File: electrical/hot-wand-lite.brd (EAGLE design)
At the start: 112 x 72 mm, 73 parts, among them IC1 12V R-78K12-2.0, IC2 AMS1117-5.0, Q1 NCHAN, Q2 SIRS5800DP-T1-GE3, Q3 DMTH64M2LPDWQ-13, Q4 2N7002K, U1 SEEED-XIAO-SAMD21, U2 1EDN8511BXUSA1, U3 LM74700QDBVTQ1, U4 AP53781

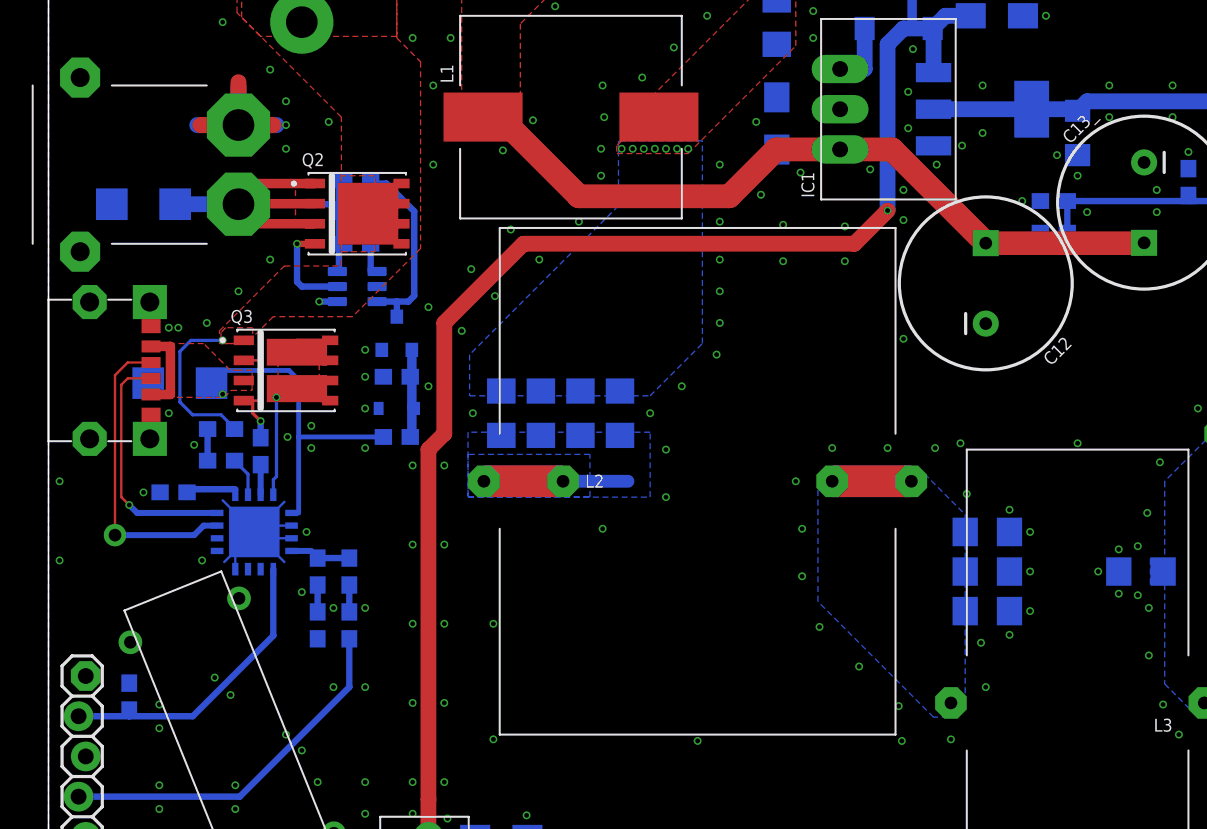
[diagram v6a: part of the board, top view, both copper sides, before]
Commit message: names and part numbers
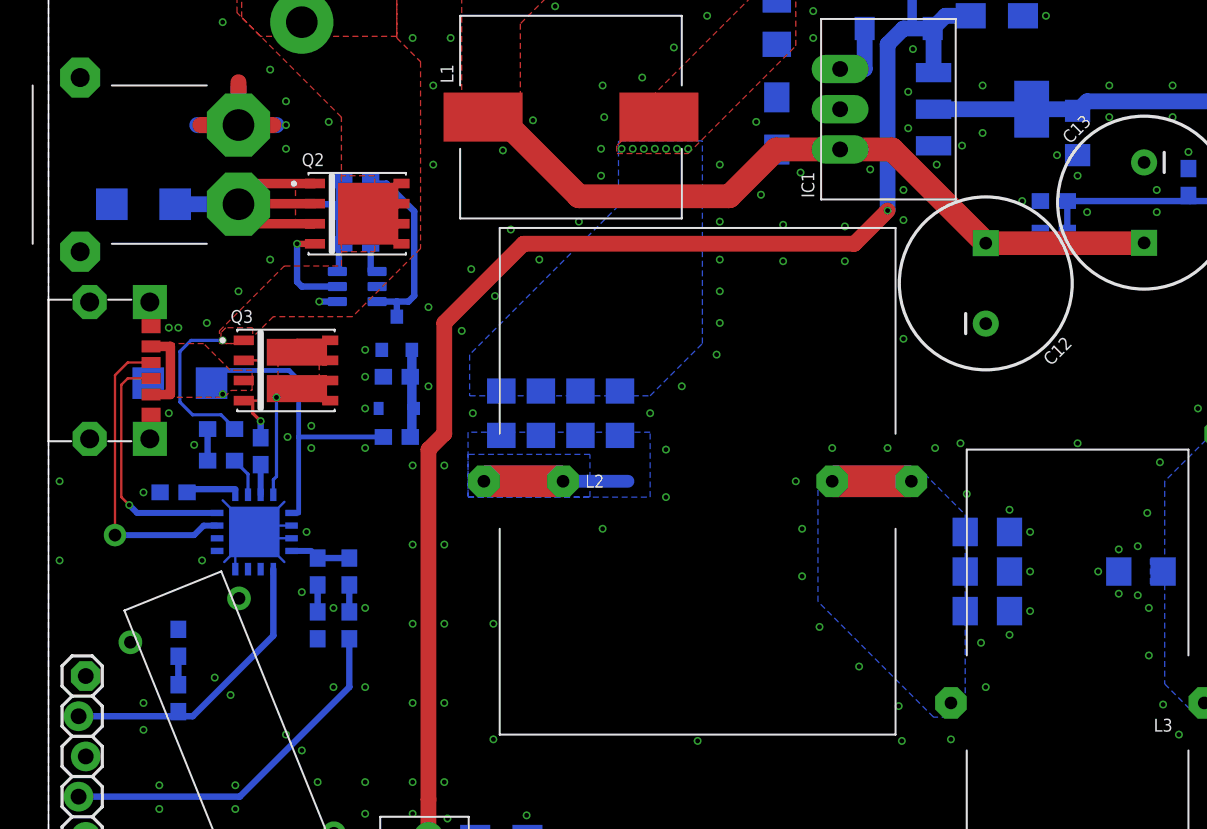
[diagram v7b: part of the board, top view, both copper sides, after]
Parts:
- removed C13_: 470u, hot-wand:CPOL-RADIAL-1000UF-25V
- removed R17_: 1K, hot-wand:0603-RES
- added C23: 100n, hot-wand:0603-CAP
- added R15: 51K, hot-wand:0603-RES
- added R7: 4K7, hot-wand:0603-RES
- C13: value 10u -> 470u; device hot-wand:EIA3216-KIT -> hot-wand:CPOL-RADIAL-1000UF-25V
- C15: device hot-wand:EIA3216 -> hot-wand:EIA3216-KIT
- C16: device hot-wand:EIA3216-KIT -> hot-wand:EIA3216
- C17: value 100n -> 10u; device hot-wand:0603-CAP -> hot-wand:EIA3216-KIT
- C18: value 1uF -> 100n
- C19: value 100n -> 1uF
- R10: value 4K7 -> 100Ω
- R11: value 4K3 -> 100Ω
- R12: value 100Ω -> 4K7
- R13: value 100Ω -> 24K
- R14: value 4K7 -> 2K
- R16: value 51K -> 1K
- R8: value 26K -> 4K7
- R9: value 4K7 -> 4K3
- moved C22 67.0 mm to (7.90, 32.3), turned to 180 degrees
- moved C17 62.1 mm to (28.6, 10.5)
- moved C16 57.5 mm to (65.0, 55.0), turned to 90 degrees
- moved C19 38.8 mm to (55.4, 64.6)
- moved R14 31.3 mm to (8.20, 22.8), turned to 90 degrees
- moved C13 23.7 mm to (69.2, 50.6), flipped to the top
- moved R8 23.5 mm to (22.0, 35.8), turned to 180 degrees
- moved R12 19.7 mm to (19.5, 52.0)
- moved C21 19.5 mm to (19.5, 48.0)
- moved R13 17.2 mm to (8.20, 19.3), turned to 90 degrees
- moved C14 15.5 mm to (46.0, 55.6), turned to 270 degrees
- moved R10 11.2 mm to (10.9, 34.3)
- moved R9 9.80 mm to (13.4, 34.9), turned to 270 degrees
- moved C15 8.99 mm to (59.9, 62.4), turned to 0 degrees
- moved R16 3.40 mm to (17.0, 23.9)
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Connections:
- new net N$10: R13.2, R14.1
- net +12V: now also C15.A, C17.A, C19.2; no longer C14.A, C16.A, C17.2
- net +24V: now also C13.1, C14.A; no longer C13.A, C13_.1
- net 5V: now also C16.A; no longer C15.A
- net ADC: now also C23.2; no longer C22.2
- net DC-SRC: now also R11.1; no longer R13.1
- net GND: now also C13.2, C17.C, C20.1, C23.1, R14.2, R16.2, R7.1; no longer C13.C, C13_.2, C17.1, C21.1, R17_.2, R8.2, R9.1
- net N$30: now also R7.2, R8.2; no longer R10.2, R9.2
- net N$31: now also C20.2, C21.1, R12.1; no longer C19.2, C20.1, R14.1
- net N$32: now also C21.2; no longer C20.2
- net N$36: now also R9.2; no longer R11.2
- net N$37: now also R9.1; no longer R11.1
- net N$38: now also C22.2; no longer C21.2
- net N$39: now also R8.1; no longer R10.1
- net N$40: now also R10.2; no longer R12.2
- net N$42: now also R15.1; no longer R16.1
- net N$43: now also R12.2; no longer R14.2
- net N$57: now also R10.1, R11.2; no longer R12.1, R13.2
- net N$9: now also R15.2, R16.1; no longer R16.2, R17_.1
- net USB-I-SEL: now also R13.1; no longer R8.1
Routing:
- net N$10: track 0.00 -> 1.80 mm

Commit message: lite, meas resistors
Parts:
- added SJ1, SJ2, SJ3, SJ4, SJ5: SJ-SMALL-1206-SJ, hot-wand:1206-SJ
- moved LED1 4.00 mm to (111.0, 45.3)
- moved LED2 4.00 mm to (111.0, 45.3)
- moved R5 4.00 mm to (110.4, 48.3)
- moved R6 4.00 mm to (108.4, 48.3)
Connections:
- new net N$11: Q1.3, Q1.3B, SJ1.2
- new net N$12: JP1.2_1, JP1.2_2, JP1.3_1, JP1.3_2, SJ2.1, SJ3.1, SJ4.1, SJ5.1
- net GND: now also SJ1.1, SJ2.2, SJ3.2, SJ4.2, SJ5.2; no longer JP1.2_1, JP1.2_2, JP1.3_1, JP1.3_2, Q1.3, Q1.3B
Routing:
- net N$12: track 0.00 -> 17.3 mm
- net N$11: track 0.00 -> 7.30 mm
- net GND: track 51.4 -> 58.6 mm, vias 336 -> 333
- net LED: track 31.7 -> 27.7 mm
- net N$4: vias 0 -> 3
- added copper zone on layer 1, net N$4
- added copper zone on layer 1, net N$5
- added copper zone on layer 1, net N$6
